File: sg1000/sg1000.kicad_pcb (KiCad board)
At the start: 2 copper layers, 18 x 58 mm, 3 parts, among them J1 Sega_GG_Cartridge, J2 Sega_SMS_Cartridge

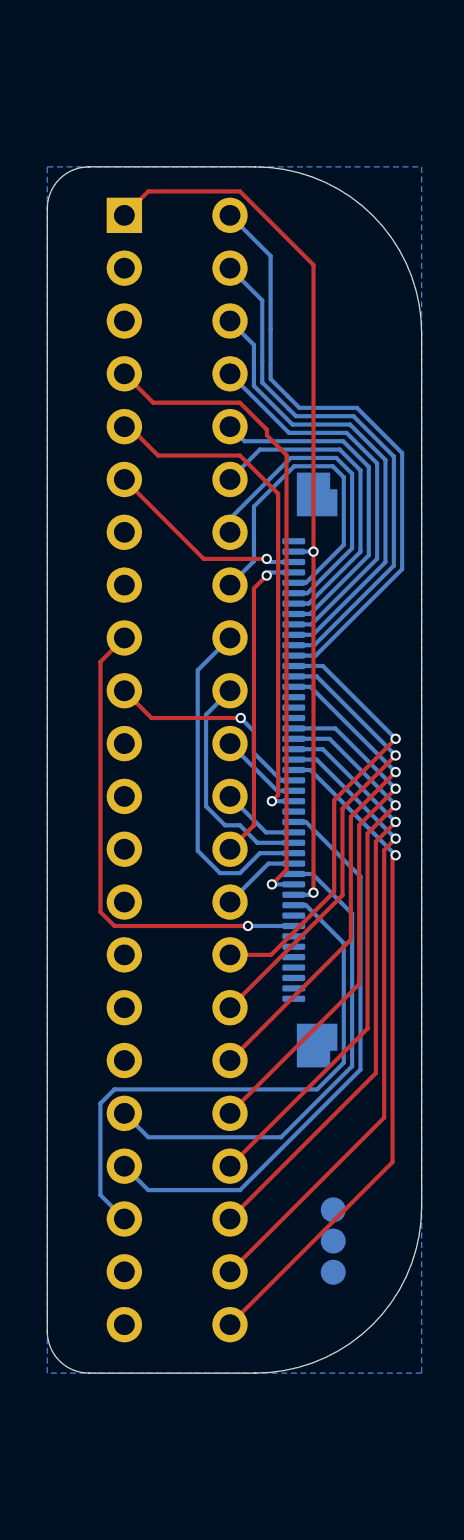
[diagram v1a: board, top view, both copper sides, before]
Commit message: Fix SG-1000 adapter slot pitch
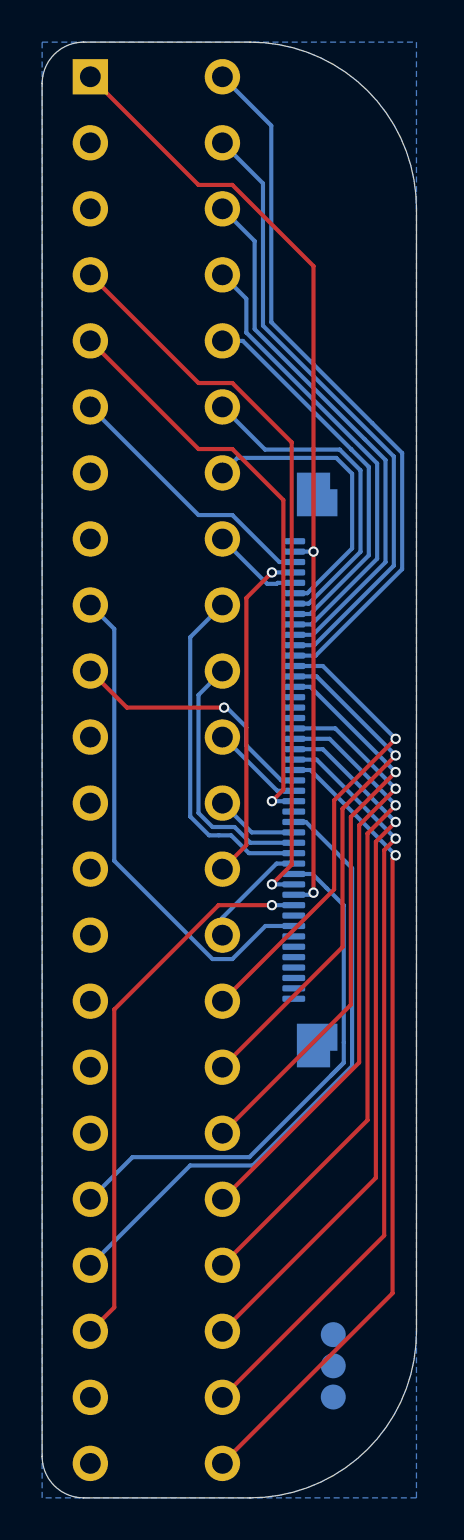
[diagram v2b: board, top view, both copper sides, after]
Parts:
- J2: footprint SugarBub:EDAC_395-044-521-802 -> SugarBub:EDAC_346-044-560-204
- moved J2 6.86 mm to (97.8, 66.7)
- moved TP1 6.00 mm to (109.5, 128.7)
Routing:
- net /A7: track 16.0 -> 4.35 mm
- net /D7: track 32.5 -> 39.3 mm
- net /D6: track 30.6 -> 36.8 mm
- net /D5: track 28.7 -> 34.3 mm
- net /A0: track 29.0 -> 34.2 mm
- net /D4: track 26.9 -> 31.8 mm
- net /A1: track 25.6 -> 30.1 mm
- net /D3: track 25.0 -> 29.3 mm
- net /M8-B: track 31.6 -> 35.7 mm
- net /A2: track 22.2 -> 26.1 mm
- net /D2: track 23.8 -> 27.4 mm
- net /RD: track 24.7 -> 28.2 mm
- net +5V: track 43.2 -> 46.6 mm
- net /A3: track 18.8 -> 22.1 mm
- net /WR: track 9.79 -> 12.9 mm, vias 1 -> 0
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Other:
- board size 18 x 58 mm -> 18 x 70 mm
